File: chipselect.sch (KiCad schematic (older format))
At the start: 6 parts, among them U12 74LS138, U13 74LS30, U14 74LS30

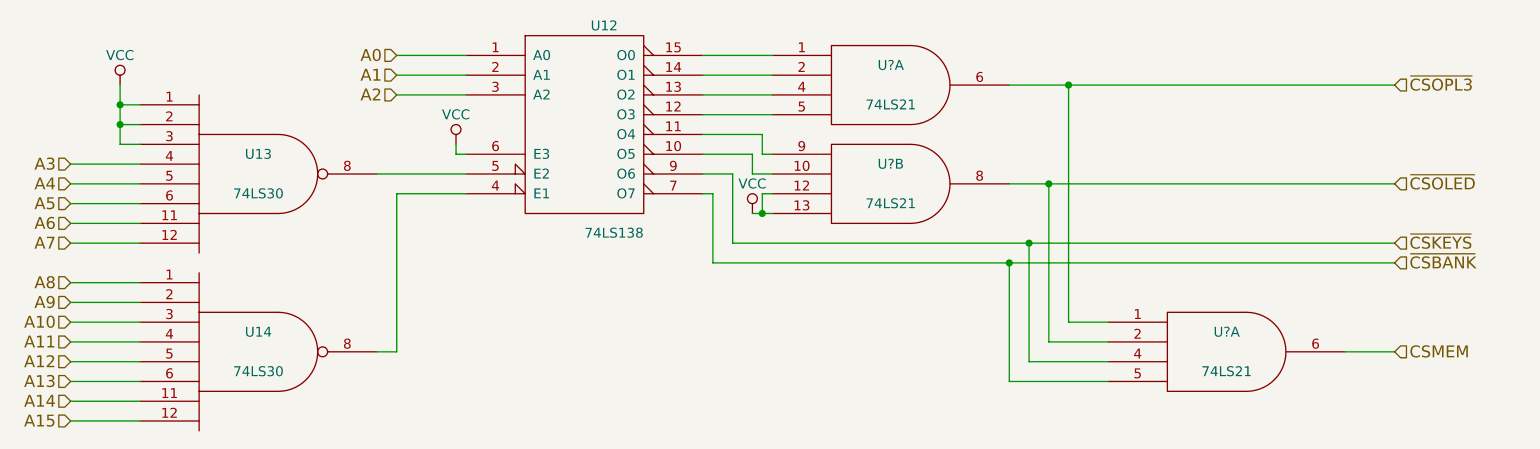
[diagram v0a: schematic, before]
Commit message: add more circuitry to schematic
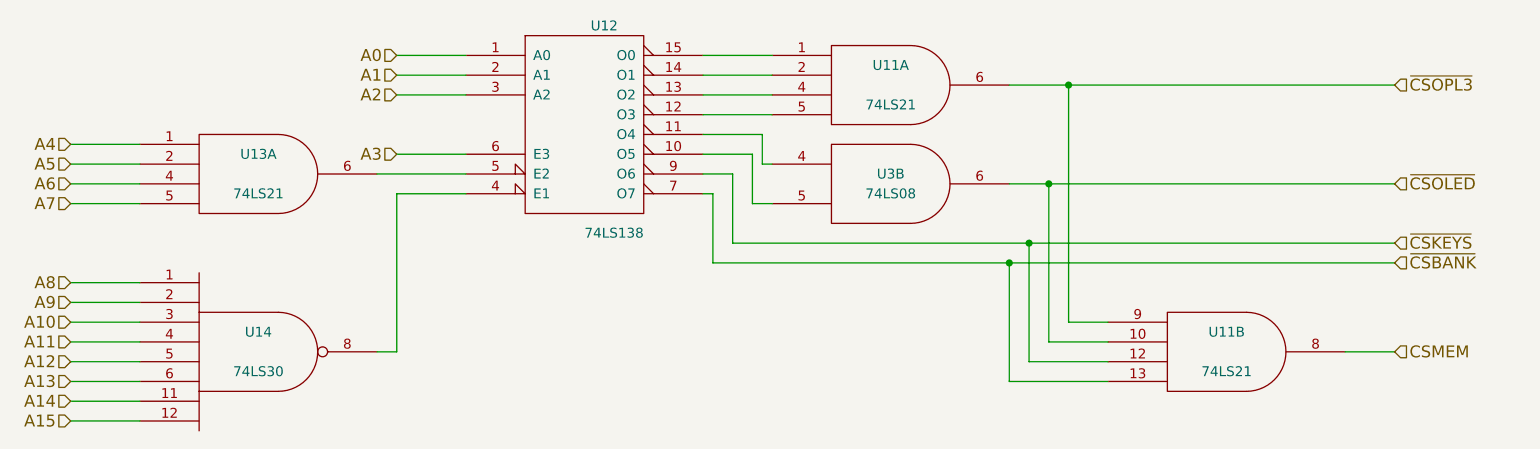
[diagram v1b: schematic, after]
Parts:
- removed U13: 74LS30, symbol 74LS30
- removed U?: 74LS21, symbol 74LS21
- added unit 2 of U11
- added U3: 74LS08, symbol 74LS08
- gave numbers to parts that had none: 2
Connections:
- net A3: now also U12.6 (E3)
- net A4: now also U13.1
- net A5: now also U13.2
- net A6: now also U13.4
- net A7: now also U13.5
- net CSMEM: now also U11.8; no longer U13.6
- net GND: now also U11.7 (GND), U3.7 (GND)
- net VCC: now also U11.14 (VCC), U3.14 (VCC); no longer U12.6 (E3)
- net ~CSBANK: now also U11.13; no longer U13.5
- net ~CSKEYS: now also U11.12; no longer U13.4
- net ~CSOLED: now also U11.10, U3.6; no longer U13.2
- net ~CSOPL3: now also U11.9; no longer U13.1
- net at U12.5 (E2): now also U13.6
- net at U12.10 (O5): now also U3.5
- net at U12.11 (O4): now also U3.4
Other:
- moved on the sheet: U13A
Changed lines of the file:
@@
 $EndDescr
-$Comp
-L 74LS30 U13
-U 1 1 5747AB76
-P 3400 3800
-F 0 "U13" H 3400 3900 50  0000 C CNN
-F 1 "74LS30" H 3400 3700 50  0000 C CNN
-F 2 "" H 3400 3800 50  0000 C CNN
-F 3 "" H 3400 3800 50  0000 C CNN
-	1    3400 3800
-	1    0    0    -1
-$EndComp
 $Comp
 L 74LS30 U14
@@
 Text HLabel 4100 3400 0    60   Input ~ 0
 A2
+Text HLabel 4100 3700 0    60   Input ~ 0
+A3
+Text HLabel 2450 3650 0    60   Input ~ 0
+A4
 Text HLabel 2450 3750 0    60   Input ~ 0
-A3
+A5
 Text HLabel 2450 3850 0    60   Input ~ 0
-A4
+A6
 Text HLabel 2450 3950 0    60   Input ~ 0
-A5
-Text HLabel 2450 4050 0    60   Input ~ 0
-A6
-Text HLabel 2450 4150 0    60   Input ~ 0
 A7
 Text HLabel 2450 4350 0    60   Input ~ 0
@@
 Text HLabel 9150 4250 2    60   Input ~ 0
 ~CSBANK
-$Comp
-L VCC #PWR5
-U 1 1 574E84CC
-P 2700 3350
-F 0 "#PWR5" H 2700 3200 50  0001 C CNN
-F 1 "VCC" H 2700 3500 50  0000 C CNN
-F 2 "" H 2700 3350 50  0000 C CNN
-F 3 "" H 2700 3350 50  0000 C CNN
-	1    2700 3350
-	1    0    0    -1
-$EndComp
-$Comp
-L VCC #PWR6
-U 1 1 574E85AD
-P 4400 3650
-F 0 "#PWR6" H 4400 3500 50  0001 C CNN
-F 1 "VCC" H 4400 3800 50  0000 C CNN
-F 2 "" H 4400 3650 50  0000 C CNN
-F 3 "" H 4400 3650 50  0000 C CNN
-	1    4400 3650
-	1    0    0    -1
-$EndComp
-Connection ~ 2700 3450
-Wire Wire Line
-	2700 3650 2800 3650
-Wire Wire Line
-	4400 3700 4450 3700
-Wire Wire Line
-	4400 3650 4400 3700
-Connection ~ 2700 3550
-Wire Wire Line
-	2800 3450 2700 3450
-Wire Wire Line
-	2700 3550 2800 3550
-Wire Wire Line
-	2700 3350 2700 3650
 Wire Wire Line
 	8900 4700 9150 4700
@@
 	2450 4350 2800 4350
 Wire Wire Line
-	2800 4150 2450 4150
-Wire Wire Line
-	2450 4050 2800 4050
-Wire Wire Line
-	2450 3950 2800 3950
-Wire Wire Line
-	2800 3850 2450 3850
+	2800 3950 2450 3950
+Wire Wire Line
+	2450 3850 2800 3850
 Wire Wire Line
 	2450 3750 2800 3750
 Wire Wire Line
+	2800 3650 2450 3650
+Wire Wire Line
+	4100 3700 4450 3700
+Wire Wire Line
 	4100 3400 4450 3400
 Wire Wire Line
@@
 	4100 3200 4450 3200
 $Comp
-L 74LS21 U?
+L 74LS21 U11
 U 1 1 575B3FEE
 P 6600 3350
-F 0 "U?" H 6600 3450 50  0000 C CNN
+F 0 "U11" H 6600 3450 50  0000 C CNN
 F 1 "74LS21" H 6600 3250 50  0000 C CNN
 F 2 "" H 6600 3350 50  0000 C CNN
@@
 $EndComp
 $Comp
-L 74LS21 U?
-U 2 1 575B40C6
+L 74LS21 U13
+U 1 1 575B4C7F
+P 3400 3800
+F 0 "U13" H 3400 3900 50  0000 C CNN
+F 1 "74LS21" H 3400 3700 50  0000 C CNN
+F 2 "" H 3400 3800 50  0000 C CNN
+F 3 "" H 3400 3800 50  0000 C CNN
+	1    3400 3800
+	1    0    0    -1
+$EndComp
+Text HLabel 9150 4150 2    60   Input ~ 0
+~CSKEYS
+Wire Wire Line
+	5650 3200 6000 3200
+Wire Wire Line
+	6000 3300 5650 3300
+Wire Wire Line
+	5650 3400 6000 3400
+Wire Wire Line
+	6000 3500 5650 3500
+Wire Wire Line
+	5650 3700 5900 3700
+Wire Wire Line
+	5900 3700 5900 3950
+Wire Wire Line
+	5650 3800 5800 3800
+Wire Wire Line
+	5800 3800 5800 4150
+Wire Wire Line
+	5650 3900 5700 3900
+Wire Wire Line
+	5700 3900 5700 4250
+Wire Wire Line
+	5800 4150 9150 4150
+Wire Wire Line
+	7200 3850 9150 3850
+Wire Wire Line
+	7200 3350 9150 3350
+Wire Wire Line
+	5700 4250 9150 4250
+Wire Wire Line
+	7200 4250 7200 4850
+Wire Wire Line
+	7200 4850 7700 4850
+Connection ~ 7200 4250
+Wire Wire Line
+	7300 4150 7300 4750
+Wire Wire Line
+	7300 4750 7700 4750
+Connection ~ 7300 4150
+Wire Wire Line
+	7700 4650 7400 4650
+Wire Wire Line
+	7400 4650 7400 3850
+Connection ~ 7400 3850
+Wire Wire Line
+	7700 4550 7500 4550
+Wire Wire Line
+	7500 4550 7500 3350
+Connection ~ 7500 3350
+$Comp
+L 74LS08 U3
+U 2 1 5770C4BF
 P 6600 3850
-F 0 "U?" H 6600 3950 50  0000 C CNN
-F 1 "74LS21" H 6600 3750 50  0000 C CNN
+F 0 "U3" H 6600 3900 50  0000 C CNN
+F 1 "74LS08" H 6600 3800 50  0000 C CNN
 F 2 "" H 6600 3850 50  0000 C CNN
 F 3 "" H 6600 3850 50  0000 C CNN
@@
 	1    0    0    -1
 $EndComp
-$Comp
-L 74LS21 U?
-U 1 1 575B4C7F
+Wire Wire Line
+	5650 3600 5950 3600
+Wire Wire Line
+	5950 3600 5950 3750
+Wire Wire Line
+	5950 3750 6000 3750
+Wire Wire Line
+	5900 3950 6000 3950
+$Comp
+L 74LS21 U11
+U 2 1 5770CB2F
 P 8300 4700
-F 0 "U?" H 8300 4800 50  0000 C CNN
+F 0 "U11" H 8300 4800 50  0000 C CNN
 F 1 "74LS21" H 8300 4600 50  0000 C CNN
 F 2 "" H 8300 4700 50  0000 C CNN
 F 3 "" H 8300 4700 50  0000 C CNN
-	1    8300 4700
-	1    0    0    -1
-$EndComp
-Text HLabel 9150 4150 2    60   Input ~ 0
-~CSKEYS
-Wire Wire Line
-	5650 3200 6000 3200
-Wire Wire Line
-	6000 3300 5650 3300
-Wire Wire Line
-	5650 3400 6000 3400
-Wire Wire Line
-	6000 3500 5650 3500
-Wire Wire Line
-	5650 3600 5950 3600
-Wire Wire Line
-	5950 3600 5950 3700
-Wire Wire Line
-	5950 3700 6000 3700
-Wire Wire Line
-	5650 3700 5900 3700
-Wire Wire Line
-	5900 3700 5900 3800
-Wire Wire Line
-	5900 3800 6000 3800
-$Comp
-L VCC #PWR?
-U 1 1 575B7163
-P 5900 4000
-F 0 "#PWR?" H 5900 3850 50  0001 C CNN
-F 1 "VCC" H 5900 4150 50  0000 C CNN
-F 2 "" H 5900 4000 50  0000 C CNN
-F 3 "" H 5900 4000 50  0000 C CNN
-	1    5900 4000
-	1    0    0    -1
-$EndComp
-Wire Wire Line
-	5900 4000 6000 4000
-Wire Wire Line
-	6000 3900 5950 3900
-Wire Wire Line
-	5950 3900 5950 4000
-Connection ~ 5950 4000
-Wire Wire Line
-	5650 3800 5800 3800
-Wire Wire Line
-	5800 3800 5800 4150
-Wire Wire Line
-	5650 3900 5700 3900
-Wire Wire Line
-	5700 3900 5700 4250
-Wire Wire Line
-	5800 4150 9150 4150
-Wire Wire Line
-	7200 3850 9150 3850
-Wire Wire Line
-	7200 3350 9150 3350
-Wire Wire Line
-	5700 4250 9150 4250
-Wire Wire Line
-	7200 4250 7200 4850
-Wire Wire Line
-	7200 4850 7700 4850
-Connection ~ 7200 4250
-Wire Wire Line
-	7300 4150 7300 4750
-Wire Wire Line
-	7300 4750 7700 4750
-Connection ~ 7300 4150
-Wire Wire Line
-	7700 4650 7400 4650
-Wire Wire Line
-	7400 4650 7400 3850
-Connection ~ 7400 3850
-Wire Wire Line
-	7700 4550 7500 4550
-Wire Wire Line
-	7500 4550 7500 3350
-Connection ~ 7500 3350
+	2    8300 4700
+	1    0    0    -1
+$EndComp
 $EndSCHEMATC
